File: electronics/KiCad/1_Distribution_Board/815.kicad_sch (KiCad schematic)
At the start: 10 parts, among them J53 Conn_01x10, J54 Conn_01x06, J55 Signals 0-3, J56 Signals 4-7, J57 Module Left, J58 Conn_02x08_Odd_Even, J59 Module Right, J60 Signals 8-11, J61 Signals 12-15

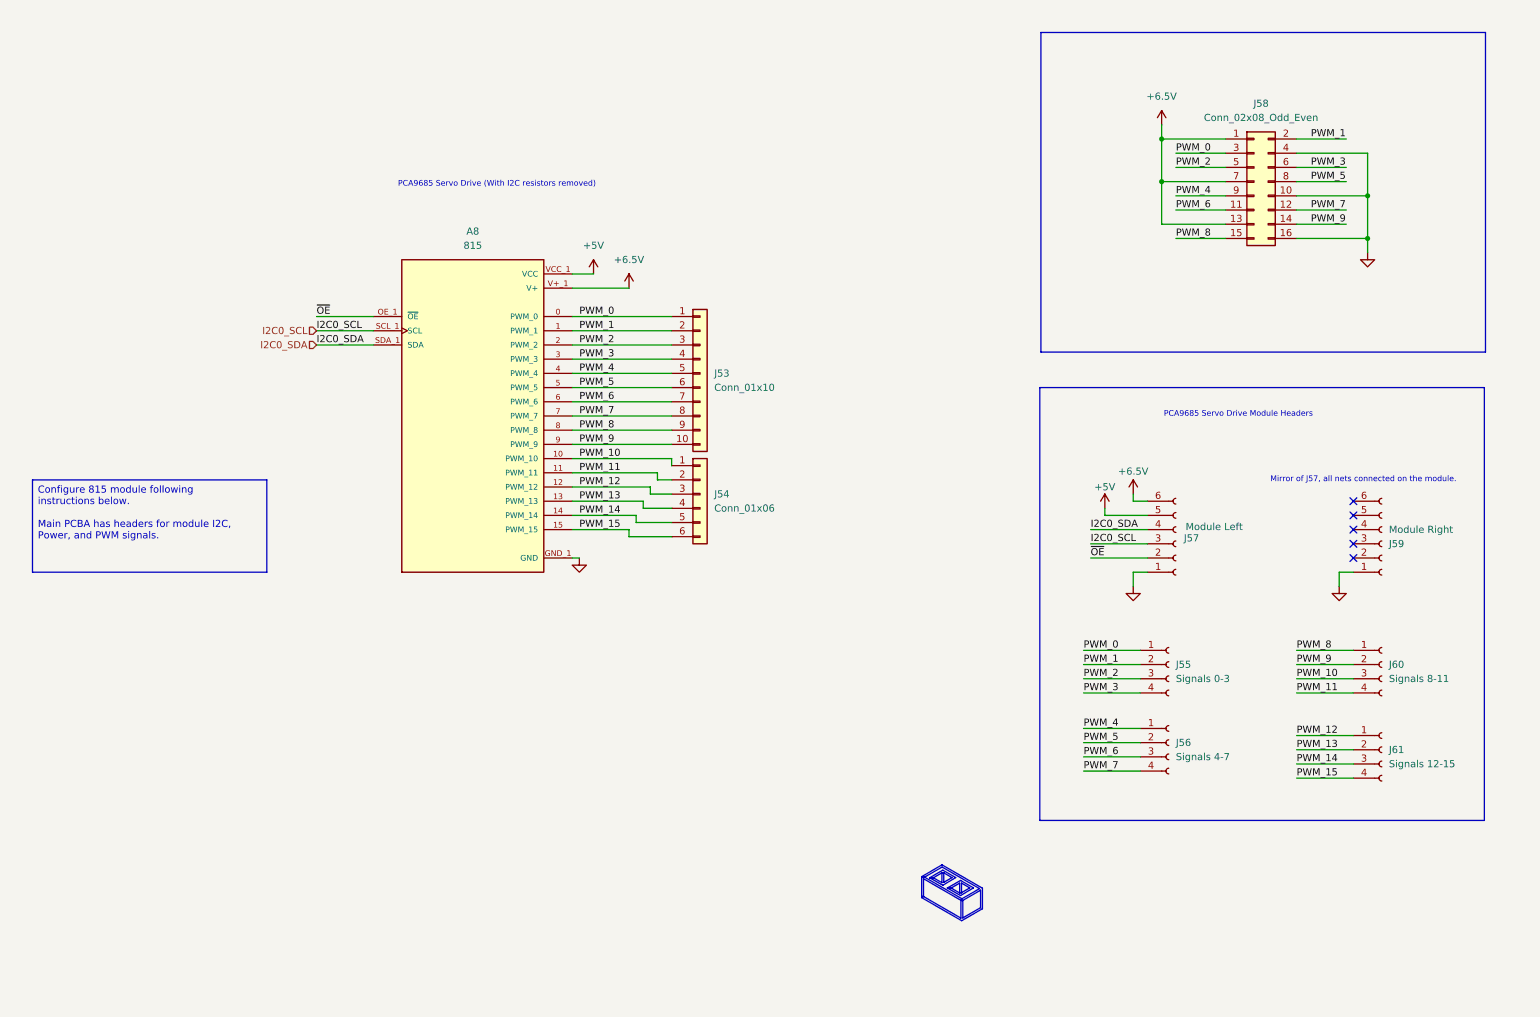
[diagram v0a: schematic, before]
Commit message: Merge board v1.3 into main (clean-clone fixups, generated files trimmed to main level) (#289)
* Initial start to updates

Removed motor pages, updated Q2,Q3, Cleaned up power module connections.

- Still need to correct routing for these updates.

* PCA Update

Updated PCA to have level shifter for I2C lines and external oscillator for precision. Corrected Power to pull from 12V.

* Removed old circuits from PCB

Removed all unused traces

* Mid work update

Lots of rework on the SCH and PCB. Checkpoint.

* Updated with more layout

Compelted PCA on board.

* adding libraries

* REV0.9 for review

Took care of all open items on the electronics PCB except for the driver resistor addresses.

* Updates Just prior to Ordering V1.0 PCBs

Updates Just prior to Ordering V1.0 PCBs

* Updates to push to V1.0

Updates to push to V1.0

* Updates to push to V1.0 missing saves. . .

Updates to push to V1.0 missing saves. . .

* Correcting Part rotation for JLCPCB

Several parts needed the "FT Rotation Offset" parameter added to correct for part orientation for JLCPCB order.

* All orientations corrected

* latest update

* Updated to reflect V1.0 of layer board as well

Updated for initial orders with PCA module populated. Also updated to layer boards for flex cables.

* Updated data and notes

* Corrected SCH for power sequence issue

5V to Vsys for all powered items.
Correction of the PCA9306 power pins.
Added decoupling to oscillator and PCA9306.

* Updated for changes to the SCH items

Updated PCB to include all changed from the SCH.

* Updated rules to correct errors

Cleaned up rules a bit to prevent false errors.

* Started work on silk update

Slowly started work on silk update.

* Corrected the 10k to 1k for connecting resistors

R1 got fixed for the correct 1k instead of 10k for UART1

* Updated Silk on PCB

Added notes for describing the pins better in the silk layer.

* Updated REV to 1.3 to reflect changes

* Updated with Version 1.3

* KiCad: make the v1.3 project 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
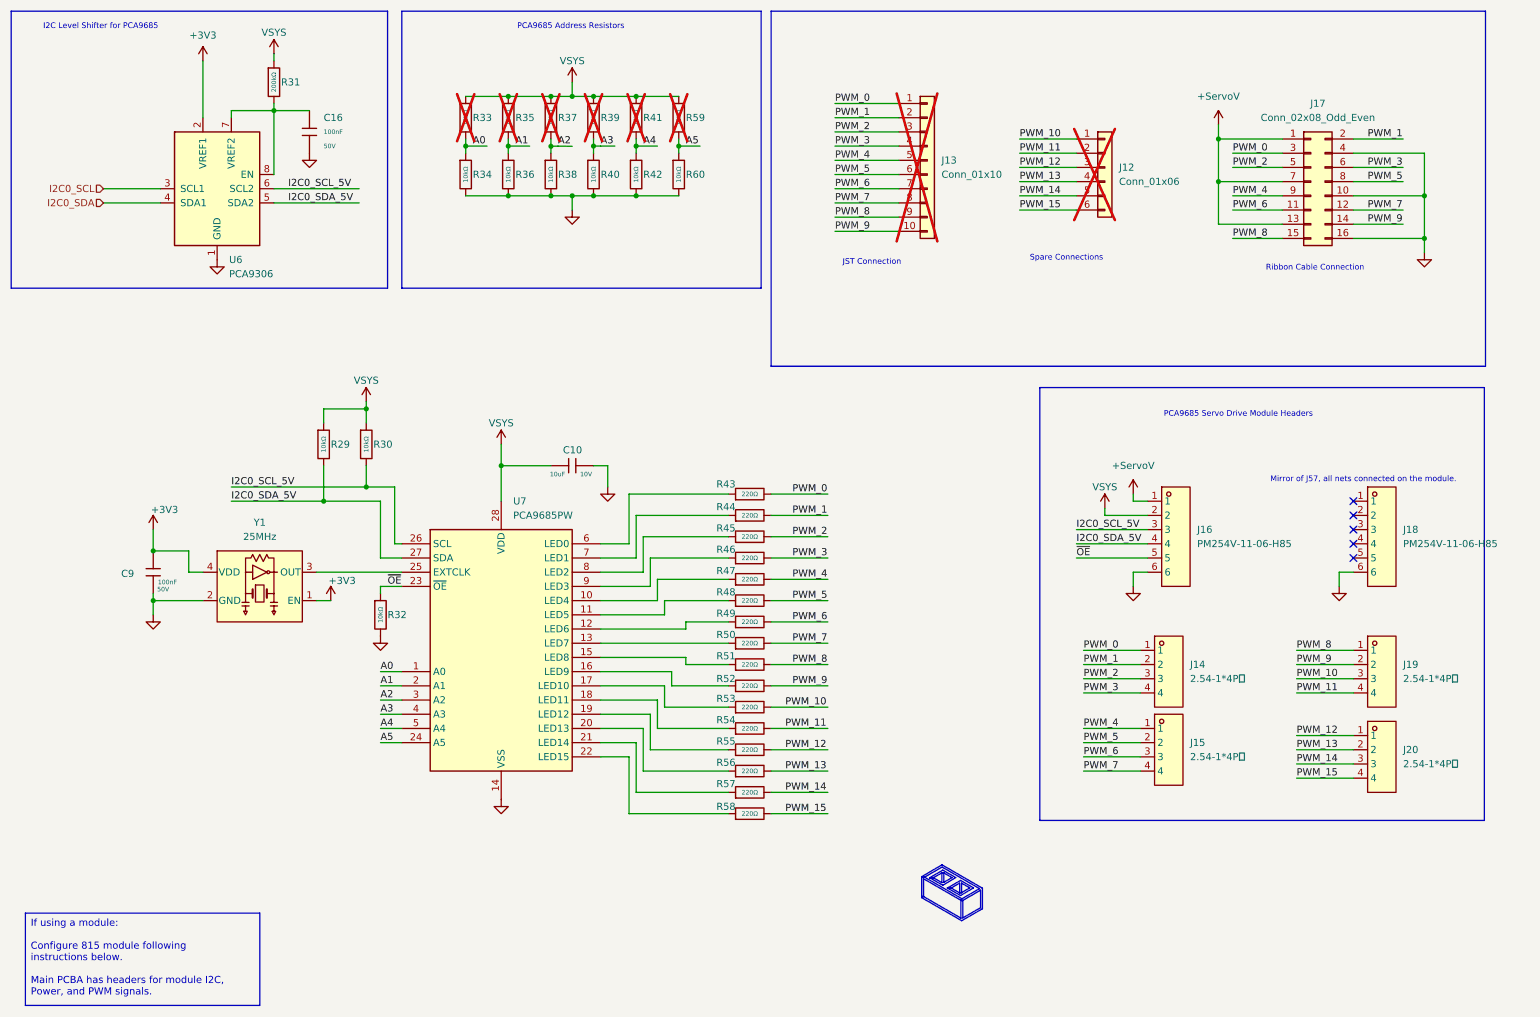
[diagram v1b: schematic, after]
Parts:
- removed A8: 815, 815:MODULE_815, symbol 815:815
- removed J55: Signals 0-3, Connector_PinSocket_2.54mm:PinSocket_1x04_P2.54mm_Vertical, symbol Connector:Conn_01x04_Socket
- removed J56: Signals 4-7, Connector_PinSocket_2.54mm:PinSocket_1x04_P2.54mm_Vertical, symbol Connector:Conn_01x04_Socket
- removed J57: Module Left, Connector_PinSocket_2.54mm:PinSocket_1x06_P2.54mm_Vertical, symbol Connector:Conn_01x06_Socket
- removed J59: Module Right, Connector_PinSocket_2.54mm:PinSocket_1x06_P2.54mm_Vertical, symbol Connector:Conn_01x06_Socket
- removed J60: Signals 8-11, Connector_PinSocket_2.54mm:PinSocket_1x04_P2.54mm_Vertical, symbol Connector:Conn_01x04_Socket
- removed J61: Signals 12-15, Connector_PinSocket_2.54mm:PinSocket_1x04_P2.54mm_Vertical, symbol Connector:Conn_01x04_Socket
- added C10: 10uF, PCM_JLCPCB:C_0603, symbol PCM_JLCPCB-Capacitors:0603,10uF
- added C16, C9: 100nF, PCM_JLCPCB:C_0603, symbol PCM_JLCPCB-Capacitors:0603,100nF
- added J14, J15, J19, J20: 2.54-1*4P母, EasyEDA:HDR-TH_4P-P2.54-V-F, symbol EasyEDA:2.54-1*4P母
- added J16, J18: PM254V-11-06-H85, EasyEDA:HDR-TH_6P-P2.54-V-F, symbol EasyEDA:PM254V-11-06-H85
- added R29, R30, R32, R33, R34, R35, R36, R37, R38, R39, R40, R41, R42, R59, R60: 10kΩ, PCM_JLCPCB:R_0603, symbol PCM_JLCPCB-Resistors:0603,10kΩ
- added R31: 200kΩ, PCM_JLCPCB:R_0603, symbol PCM_JLCPCB-Resistors:0603,200kΩ
- added R43, R44, R45, R46, R47, R48, R49, R50, R51, R52, R53, R54, R55, R56, R57, R58: 220Ω, PCM_JLCPCB:R_0603, symbol PCM_JLCPCB-Resistors:0603,220Ω
- added U6: PCA9306, Package_SO:Texas_S-PDSO-G8_3x3mm_P0.65mm, symbol Interface:PCA9306
- added U7: PCA9685PW, Package_SO:TSSOP-28_4.4x9.7mm_P0.65mm, symbol Driver_LED:PCA9685PW
- added Y1: 25MHz, Crystal_SMD_3.2x2.5mm, symbol PCM_SparkFun-Clock:Oscillator_24MHz_3.2x2.5mm
- J12: renamed from J54; LCSC (none) -> C37208; now not fitted
- J13: renamed from J53; LCSC (none) -> C378928; now not fitted
- J17: renamed from J58; LCSC (none) -> C429960
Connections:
- net GND: now also C10.2, C16.2, C9.1, J16.6, J18.6, R32.2, R34.2, R36.2, R38.2, R40.2, R42.2, R60.2, U6.1 (GND), U7.14 (VSS), Y1.2 (GND)
- net I2C0_SCL: now also U6.3 (SCL1)
- net I2C0_SDA: now also U6.4 (SDA1)
- net PWM_0: now also J14.1, R43.2
- net PWM_1: now also J14.2, R44.2
- net PWM_10: now also J19.3, R53.2
- net PWM_11: now also J19.4, R54.2
- net PWM_12: now also J20.1, R55.2
- net PWM_13: now also J20.2, R56.2
- net PWM_14: now also J20.3, R57.2
- net PWM_15: now also J20.4, R58.2
- net PWM_2: now also J14.3, R45.2
- net PWM_3: now also J14.4, R46.2
- net PWM_4: now also J15.1, R47.2
- net PWM_5: now also J15.2, R48.2
- net PWM_6: now also J15.3, R49.2
- net PWM_7: now also J15.4, R50.2
- net PWM_8: now also J19.1, R51.2
- net PWM_9: now also J19.2, R52.2
- net ~{OE}: now also J16.5, R32.1, U7.23 (~{OE})
- net +6.5V renamed +ServoV
- net +ServoV: now also J16.1
- new net: R53.1, U7.17 (LED10)
- new net: R47.1, U7.10 (LED4)
- new net: R48.1, U7.11 (LED5)
- new net: R49.1, U7.12 (LED6)
- new net: R50.1, U7.13 (LED7)
- new net: R51.1, U7.15 (LED8)
- new net: R52.1, U7.16 (LED9)
- new net: R54.1, U7.18 (LED11)
- new net: R55.1, U7.19 (LED12)
- new net: R56.1, U7.20 (LED13)
- new net: R57.1, U7.21 (LED14)
- new net: R58.1, U7.22 (LED15)
- new net: U7.25 (EXTCLK), Y1.3 (OUT)
- new net: R43.1, U7.6 (LED0)
- new net: R44.1, U7.7 (LED1)
- new net: R45.1, U7.8 (LED2)
- new net: R46.1, U7.9 (LED3)
- new net: C16.1, R31.2, U6.7 (VREF2), U6.8 (EN)
- new net +3V3: C9.2, U6.2 (VREF1), Y1.1 (EN), Y1.4 (VDD)
- new net A0: R33.2, R34.1, U7.1 (A0)
- new net A1: R35.2, R36.1, U7.2 (A1)
- new net A2: R37.2, R38.1, U7.3 (A2)
- new net A3: R39.2, R40.1, U7.4 (A3)
- new net A4: R41.2, R42.1, U7.5 (A4)
- new net A5: R59.2, R60.1, U7.24 (A5)
- new net I2C0_SCL_5V: J16.3, R30.2, U6.6 (SCL2), U7.26 (SCL)
- new net I2C0_SDA_5V: J16.4, R29.2, U6.5 (SDA2), U7.27 (SDA)
- new net VSYS: C10.1, J16.2, R29.1, R30.1, R31.1, R33.1, R35.1, R37.1, R39.1, R41.1, R59.1, U7.28 (VDD)
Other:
- note added: "I2C Level Shifter for PCA9685"
- note added: "JST Connection"
- note added: "PCA9685 Address Resistors"
- note added: "Ribbon Cable Connection"
- note added: "Spare Connections"
- note removed: "PCA9685 Servo Drive (With I2C resistors removed)"
- moved on the sheet: J17
